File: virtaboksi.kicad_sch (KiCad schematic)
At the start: 33 parts, among them J1 Panel_01x06, J2 External_01x06, J3 Optional_01x03, J5 Powerpole 01x02, J6 Powerpole 01x02, J7 Powerpole 01x02, J8 TagConnect_TC2030-NL, Q10 MMBT3906, Q11 MMBT3906, Q12 MMBT3906, Q13 MMBT3906, U1 SRV05-4, U2 AMSRI-783.3-NZ, U3 SRV05-4, U4 SP3485EN, U5 STM8S003F3P

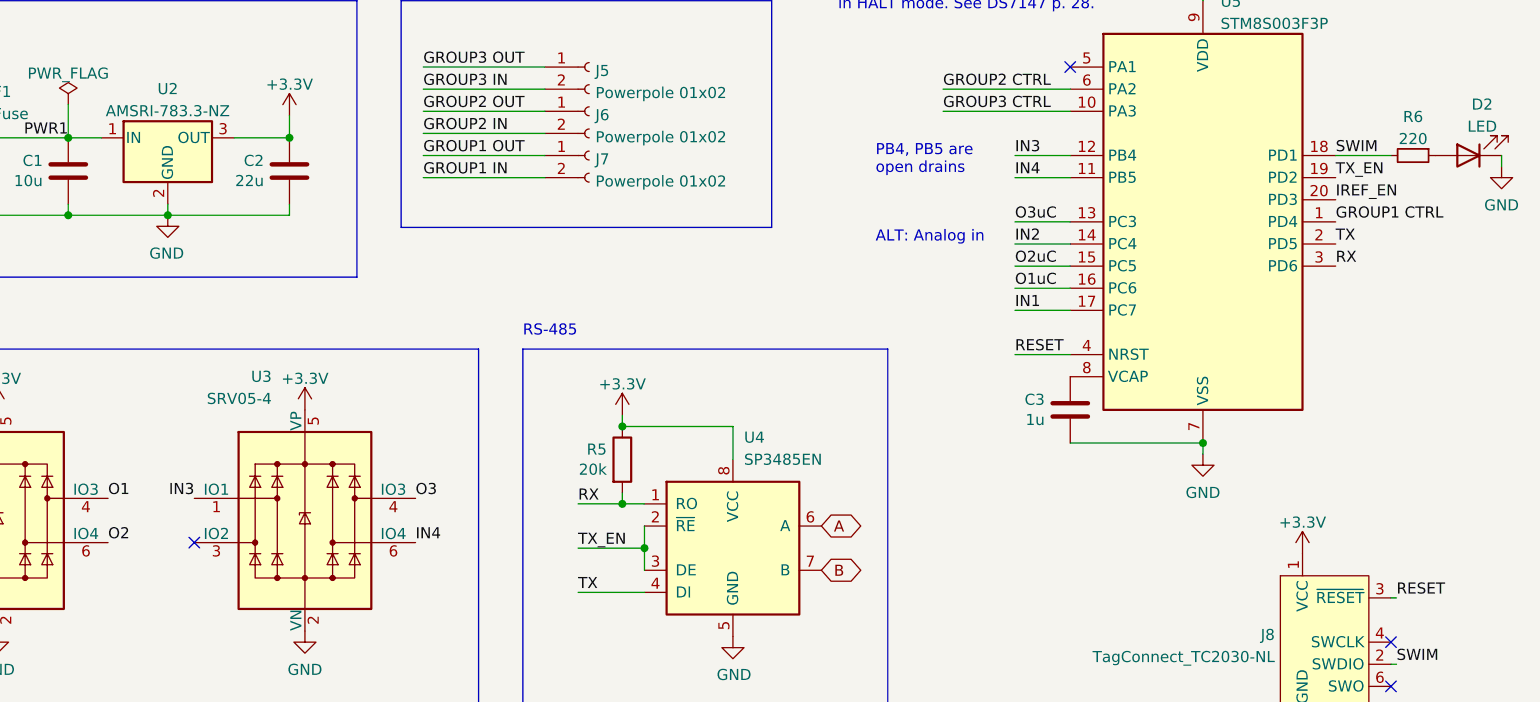
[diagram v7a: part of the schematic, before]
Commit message: Reorganize pins so that we got two analog inputs, bot I1 and I2
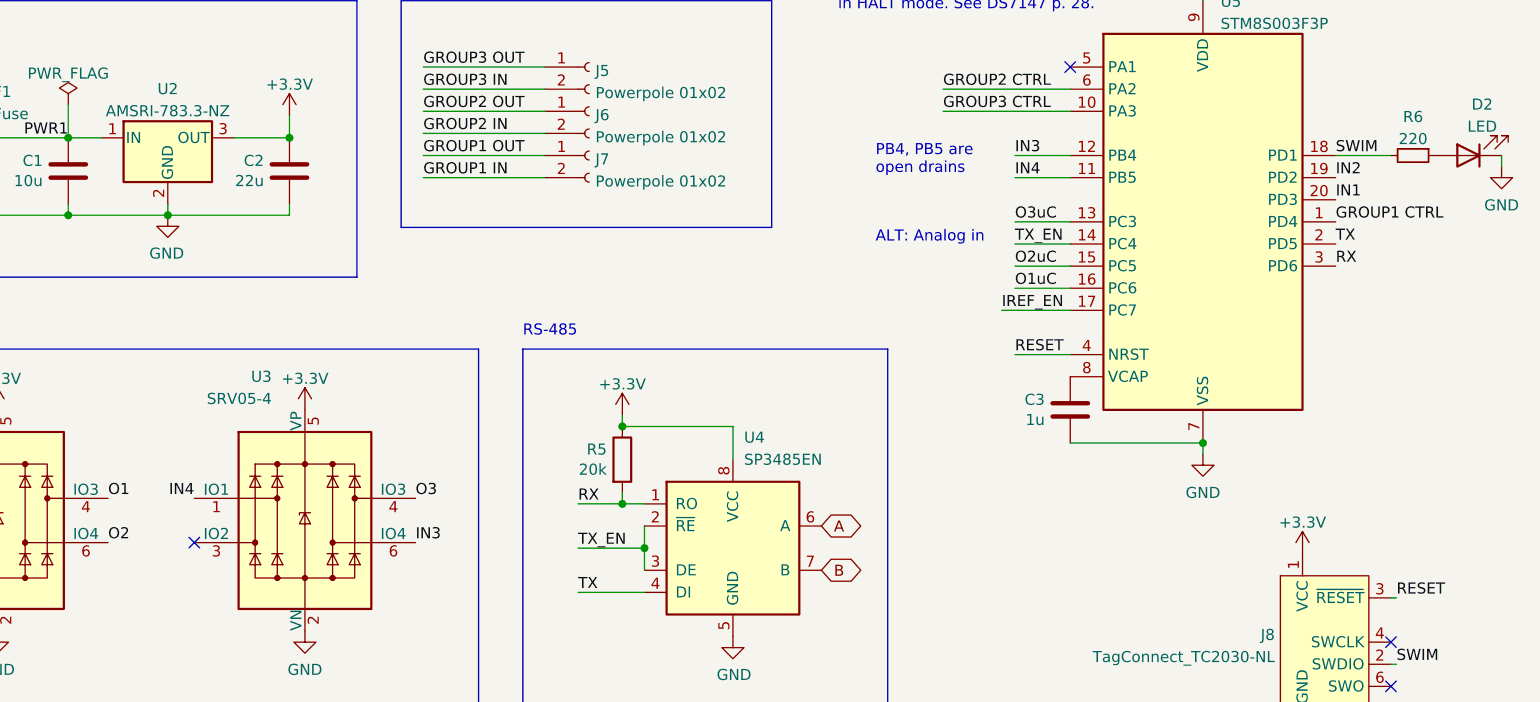
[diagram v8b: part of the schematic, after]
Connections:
- net IN1: now also U5.20 (PD3); no longer U5.17 (PC7)
- net IN2: now also U5.19 (PD2); no longer U5.14 (PC4)
- net IN3: now also U3.6 (IO4); no longer U3.1 (IO1)
- net IN4: now also U3.1 (IO1); no longer U3.6 (IO4)
- net IREF_EN: now also U5.17 (PC7); no longer U5.20 (PD3)
- net TX_EN: now also U5.14 (PC4); no longer U5.19 (PD2)
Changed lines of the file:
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@@
     (stroke (width 0) (type default) (color 0 0 0 0))
   )
-  (wire (pts (xy 224.79 57.15) (xy 231.14 57.15))
+  (wire (pts (xy 223.266 57.15) (xy 231.14 57.15))
     (stroke (width 0) (type default) (color 0 0 0 0))
   )
@@
     (effects (font (size 1.27 1.27)) (justify left bottom))
   )
-  (label "IN2" (at 224.79 49.53 0)
+  (label "IN2" (at 261.62 41.91 0)
     (effects (font (size 1.27 1.27)) (justify left bottom))
   )
@@
     (effects (font (size 1.27 1.27)) (justify left bottom))
   )
-  (label "TX_EN" (at 261.62 41.91 0)
+  (label "TX_EN" (at 224.79 49.53 0)
     (effects (font (size 1.27 1.27)) (justify left bottom))
   )
@@
     (effects (font (size 1.27 1.27)) (justify left bottom))
   )
-  (label "IN1" (at 224.79 57.15 0)
+  (label "IN1" (at 261.62 44.45 0)
     (effects (font (size 1.27 1.27)) (justify left bottom))
   )
@@
     (effects (font (size 1.27 1.27)) (justify left bottom))
   )
-  (label "IN4" (at 155.956 83.82 0)
-    (effects (font (size 1.27 1.27)) (justify left bottom))
+  (label "IN4" (at 130.556 78.74 180)
+    (effects (font (size 1.27 1.27)) (justify right bottom))
   )
   (label "IN4" (at 209.55 132.08 90)
@@
     (effects (font (size 1.27 1.27)) (justify left bottom))
   )
-  (label "IN3" (at 130.556 78.74 180)
-    (effects (font (size 1.27 1.27)) (justify right bottom))
+  (label "IN3" (at 155.956 83.82 0)
+    (effects (font (size 1.27 1.27)) (justify left bottom))
   )
   (label "IN3" (at 126.111 124.714 0)
@@
     (effects (font (size 1.27 1.27)) (justify right bottom))
   )
-  (label "IREF_EN" (at 261.62 44.45 0)
-    (effects (font (size 1.27 1.27)) (justify left bottom))
-  )
+  (label "IREF_EN" (at 223.266 57.15 0)
+    (effects (font (size 1.27 1.27)) (justify left bottom))
+  )
